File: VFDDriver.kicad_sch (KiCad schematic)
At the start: 18 parts

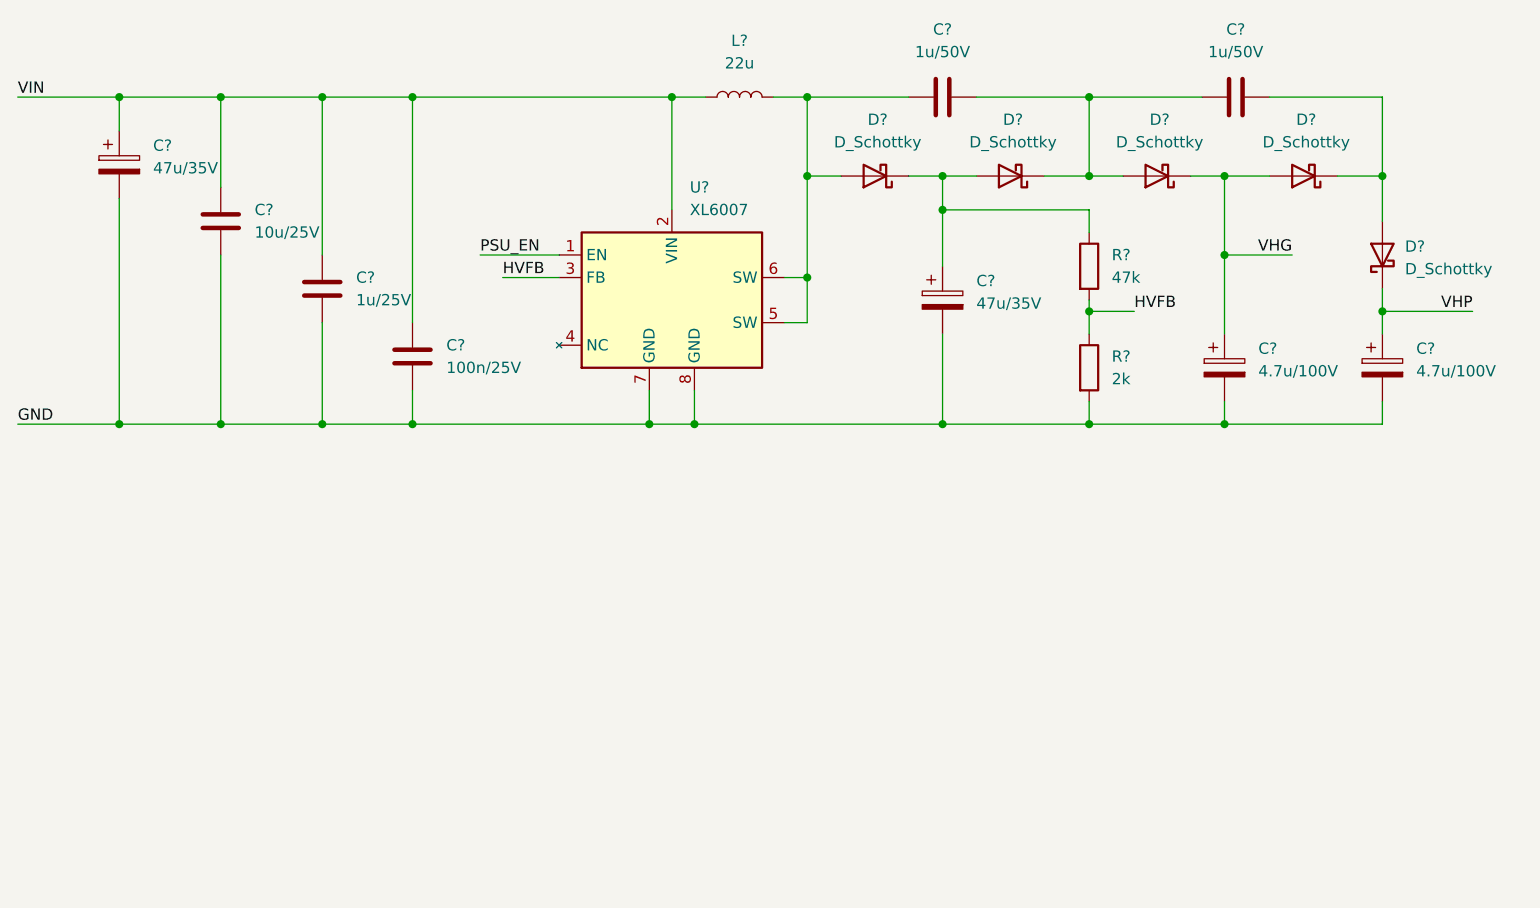
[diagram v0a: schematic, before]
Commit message: Added filament supply
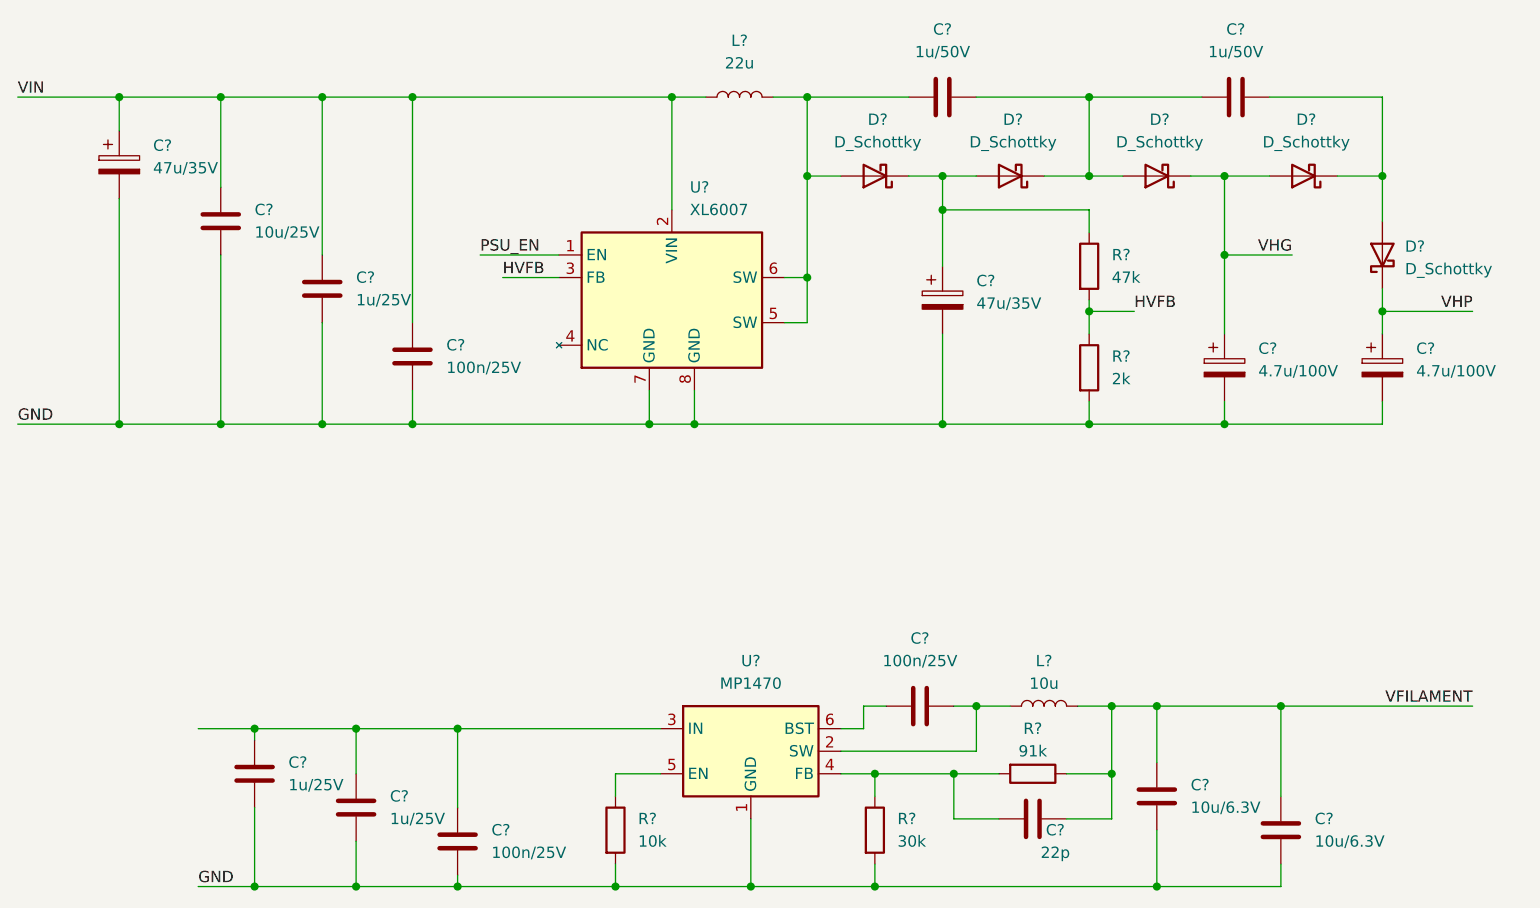
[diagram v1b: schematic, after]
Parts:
- added C? (x2): 10u/6.3V, symbol Device:C
- added C? (x2): 1u/25V, symbol Device:C
- added C? (x2): 100n/25V, symbol Device:C
- added C?: 22p, symbol Device:C
- added L?: 10u, symbol Device:L
- added R?: 91k, symbol Device:R
- added R?: 30k, symbol Device:R
- added R?: 10k, symbol Device:R
- added U?: MP1470, Package_TO_SOT_SMD:TSOT-23-6, symbol Regulator_Switching:MP1470
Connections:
- net GND: now also C?.2, C?.2, C?.2, C?.2, C?.2, R?.2, R?.2, U?.1 (GND)
- new net: C?.1, L?.1, U?.2 (SW)
- new net: C?.1, R?.1, R?.2, U?.4 (FB)
- new net: C?.1, C?.1, C?.1, U?.3 (IN)
- new net: C?.2, U?.6 (BST)
- new net: R?.1, U?.5 (EN)
- new net VFILAMENT: C?.1, C?.1, C?.2, L?.2, R?.1
